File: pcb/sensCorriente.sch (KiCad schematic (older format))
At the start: 23 parts, among them J1 I_in, J2 USB, J3 SD-CON, P1 LPCXpresso, SW1 CALIB, U1 ACS713

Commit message: Added serial interface.
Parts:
- added C10, C11, C8, C9: 100nF, ~, symbol C
- added J4: DB9F, ~, symbol DB9
- added U2: MAX232, symbol MAX232
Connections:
- net labels added: CTS1, RTS1, RXD1, TXD1
- wire segments 91 -> 124
- no-connect marks 40 -> 41
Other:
- moved on the sheet: C1, C2, C3, C4, C5, C6, C7, J1, J2, J3, R1, R2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

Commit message: Corregido footprint de RV1 y J4.
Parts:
- J4: value DB9F -> DB9
- RV1: value 10k -> POT
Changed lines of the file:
@@
 LIBS:lpcxpresso
 LIBS:sd-con
+LIBS:pot
+LIBS:db9
 LIBS:sensCorriente-cache
 EELAYER 27 0
@@
 Sheet 1 1
 Title "Sensor de Corriente"
-Date "3 sep 2014"
+Date "12 sep 2014"
 Rev "0.1"
 Comp "DPLab @ UTN-FRBA"
@@
 	6900 4850 6950 4850
 Connection ~ 6900 5250
-$Comp
-L POT RV1
-U 1 1 53FF4F26
-P 6250 5050
-F 0 "RV1" H 6250 4950 50  0000 C CNN
-F 1 "10k" H 6250 5050 50  0000 C CNN
-F 2 "~" H 6250 5050 60  0000 C CNN
-F 3 "~" H 6250 5050 60  0000 C CNN
-	1    6250 5050
-	0    1    1    0
-$EndComp
 Wire Wire Line
 	6950 5050 6400 5050
@@
 	7750 2550 7450 2550
 $Comp
-L DB9 J4
-U 1 1 5406664E
-P 10500 2350
-F 0 "J4" H 10500 2900 70  0000 C CNN
-F 1 "DB9F" H 10300 1800 70  0000 C CNN
-F 2 "~" H 10500 2350 60  0000 C CNN
-F 3 "~" H 10500 2350 60  0000 C CNN
-	1    10500 2350
-	1    0    0    -1
-$EndComp
-$Comp
 L GND #PWR027
 U 1 1 5406665B
@@
 NoConn ~ 5400 2250
 NoConn ~ 5400 2150
+$Comp
+L POT RV1
+U 1 1 54134A6D
+P 6250 5050
+F 0 "RV1" H 6250 4950 50  0000 C CNN
+F 1 "POT" H 6250 5050 50  0000 C CNN
+F 2 "~" H 6250 5050 60  0000 C CNN
+F 3 "~" H 6250 5050 60  0000 C CNN
+	1    6250 5050
+	0    1    1    0
+$EndComp
+$Comp
+L DB9 J4
+U 1 1 54134B0D
+P 10500 2350
+F 0 "J4" H 10500 2900 70  0000 C CNN
+F 1 "DB9" H 10300 1800 70  0000 C CNN
+F 2 "~" H 10500 2350 60  0000 C CNN
+F 3 "~" H 10500 2350 60  0000 C CNN
+	1    10500 2350
+	1    0    0    -1
+$EndComp
 $EndSCHEMATC

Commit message: Se realizaron cambios en el esquematico. Revisar ERC.
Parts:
- removed J3: SD-CON, sdcard, symbol SD-CON
- added C12, C13: 100nF, ~, symbol C
- added J3: CONECTORSD, sdcard, symbol CONECTORSD
- added R10, R9: 10k, ~, symbol R
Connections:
- net labels added: SD_CD, SD_WP
- wire segments 124 -> 135
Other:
- moved on the sheet: C1, C2

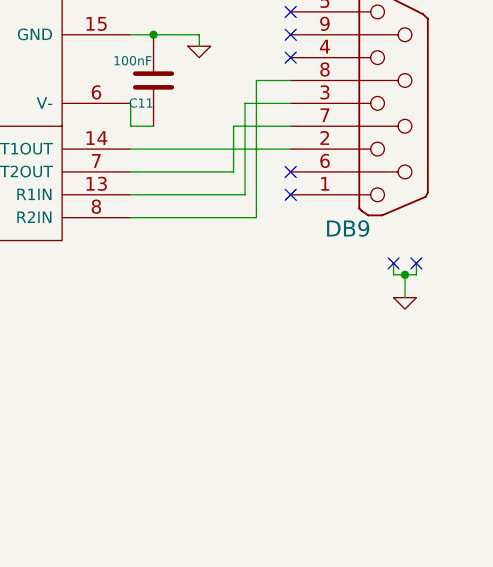
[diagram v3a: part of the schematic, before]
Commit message: Primer version del pcb terminado. Verificar y realizar correcciones. ERC OK en el esquematico y en el pcb.
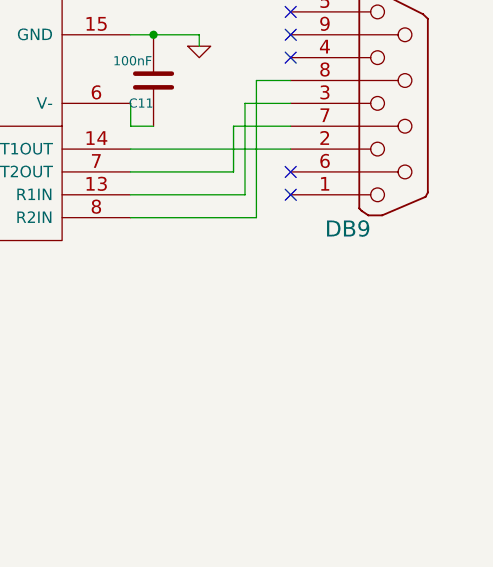
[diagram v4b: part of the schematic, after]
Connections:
- wire segments 135 -> 131
- no-connect marks 41 -> 39
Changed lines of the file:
@@
 Sheet 1 1
 Title "Sensor de Corriente"
-Date "24 oct 2014"
+Date "31 oct 2014"
 Rev "0.1"
 Comp "DPLab @ UTN-FRBA"
@@
 Text Label 7450 2750 0    60   ~ 0
 RXD1
-$Comp
-L GND #PWR027
-U 1 1 5406665B
-P 10550 3200
-F 0 "#PWR027" H 10550 3200 30  0001 C CNN
-F 1 "GND" H 10550 3130 30  0001 C CNN
-F 2 "" H 10550 3200 60  0000 C CNN
-F 3 "" H 10550 3200 60  0000 C CNN
-	1    10550 3200
-	1    0    0    -1
-$EndComp
 NoConn ~ 10050 2750
 NoConn ~ 10050 2650
@@
 	7750 2550 7450 2550
 Wire Wire Line
-	10550 3200 10550 3100
-Wire Wire Line
-	10500 3100 10600 3100
-Wire Wire Line
-	10500 3100 10500 3050
-Wire Wire Line
-	10600 3100 10600 3050
-Connection ~ 10550 3100
-Wire Wire Line
 	9350 2550 10050 2550
 Wire Wire Line
@@
 	2700 7200 2900 7200
 $Comp
-L GND #PWR028
+L GND #PWR027
 U 1 1 544AE3B6
 P 2800 7300
-F 0 "#PWR028" H 2800 7300 30  0001 C CNN
+F 0 "#PWR027" H 2800 7300 30  0001 C CNN
 F 1 "GND" H 2800 7230 30  0001 C CNN
 F 2 "" H 2800 7300 60  0000 C CNN
@@
 Connection ~ 3100 5150
 Connection ~ 2400 5150
-NoConn ~ 10500 3050
-NoConn ~ 10600 3050
 $EndSCHEMATC
